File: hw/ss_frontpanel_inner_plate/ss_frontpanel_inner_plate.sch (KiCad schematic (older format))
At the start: 32 parts, among them J1 FFC_conn_14p, J2 FFC_conn_14p, J3 FFC_conn_14p, M1 Mousebite_stamp_holes, M2 Mousebite_stamp_holes, M3 Mousebite_stamp_holes, M4 FFC_retention_clamp, M5 FFC_retention_clamp, U6 TLV9051SIDBV

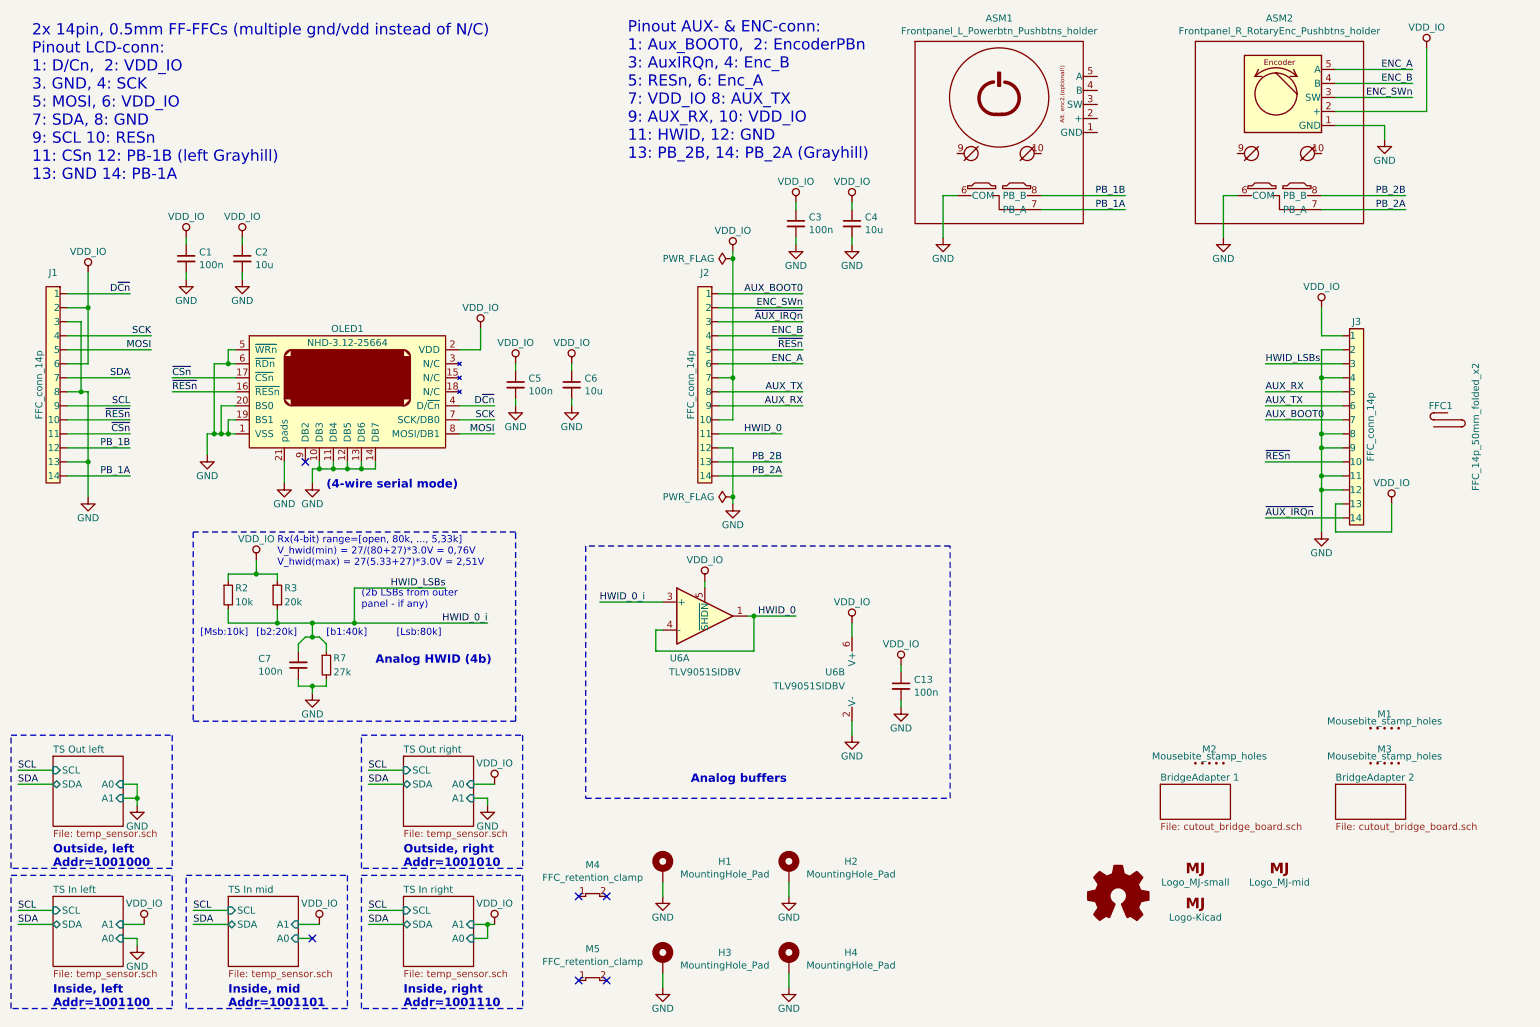
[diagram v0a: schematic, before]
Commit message: Updated display-board sch & PCB with optional left-hand rotary encoder instead of pwrbtn. Printed MB schematic updates PDF for 20-08-21
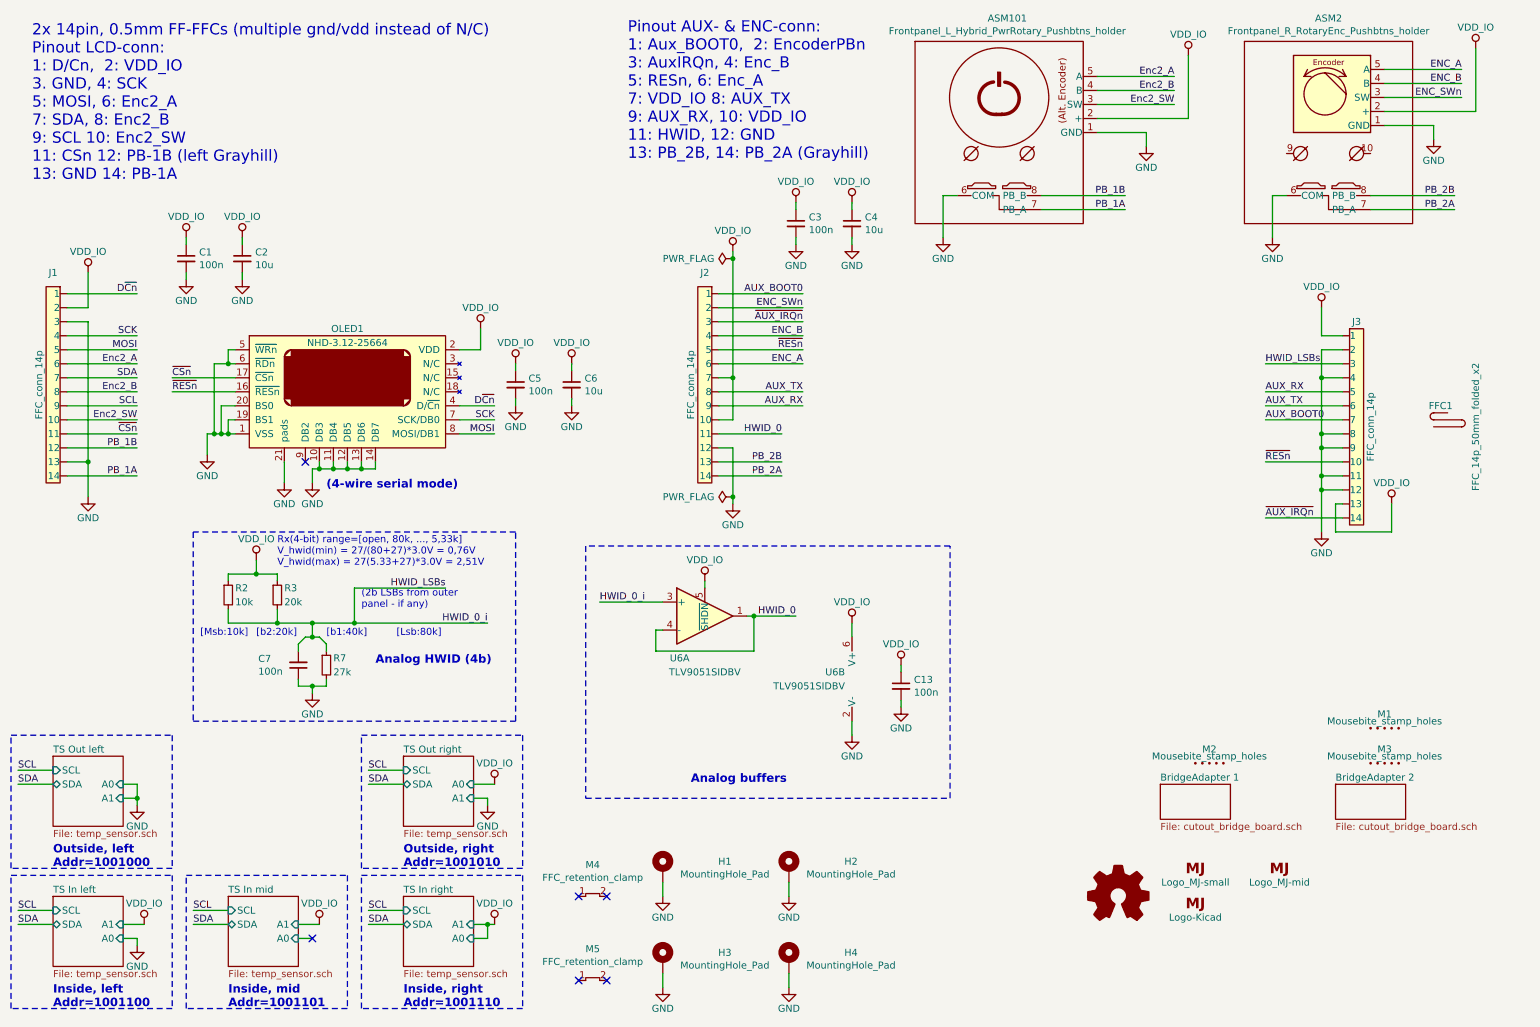
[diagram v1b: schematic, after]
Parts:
- removed ASM1: Frontpanel_L_Powerbtn_Pushbtns_holder, customlib_mj_fp:Frontpanel_L_Powerbtn_Pushbtns_holder, symbol customlib_mj:Frontpanel_L_Powerbtn_Pushbtns_holder
- added ASM101: Frontpanel_L_Hybrid_PwrRotary_Pushbtns_holder, customlib_mj_fp:Frontpanel_L_Hybrid_Power_Rotary_Pushbtns_holder, symbol customlib_mj:Frontpanel_L_Hybrid_PwrRotary_Pushbtns_holder
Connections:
- net GND: now also ASM101.1 (GND), ASM101.6 (COM); no longer J1.8
- net PB_1A: now also ASM101.7 (PB_A)
- net PB_1B: now also ASM101.8 (PB_B)
- net VDD_IO: now also ASM101.2 (+); no longer J1.6
- net ~RESn~: no longer J1.10
- new net Enc2_A: ASM101.5 (A), J1.6
- new net Enc2_B: ASM101.4 (B), J1.8
- new net Enc2_SW: ASM101.3 (SW), J1.10
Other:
- note added: "2x 14pin, 0.5mm FF-FFCs (multiple gnd/vdd instead of N/C)\nPinout LCD-conn:\n1: D/Cn, 2: VDD_IO\n3. GND, 4: SCK\n5: MOSI, 6: Enc2_A\n7: SDA, 8: Enc2_B\n9: SCL 10: Enc2_SW\n11: CSn 12: PB-1B (left Grayhill)\n13: GND 14: PB-1A"
- note removed: "2x 14pin, 0.5mm FF-FFCs (multiple gnd/vdd instead of N/C)\nPinout LCD-conn:\n1: D/Cn, 2: VDD_IO\n3. GND, 4: SCK\n5: MOSI, 6: VDD_IO\n7: SDA, 8: GND\n9: SCL 10: RESn\n11: CSn 12: PB-1B (left Grayhill)\n13: GND 14: PB-1A"
- moved on the sheet: ASM2
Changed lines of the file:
@@
 $EndDescr
 Text Notes 700  1800 0    80   ~ 0
-2x 14pin, 0.5mm FF-FFCs (multiple gnd/vdd instead of N/C)\nPinout LCD-conn:\n1: D/Cn,  2: VDD_IO\n3. GND, 4: SCK\n5: MOSI, 6: VDD_IO\n7: SDA, 8: GND\n9: SCL 10: RESn\n11: CSn 12: PB-1B (left Grayhill)\n13: GND 14: PB-1A
+2x 14pin, 0.5mm FF-FFCs (multiple gnd/vdd instead of N/C)\nPinout LCD-conn:\n1: D/Cn,  2: VDD_IO\n3. GND, 4: SCK\n5: MOSI, 6: Enc2_A\n7: SDA, 8: Enc2_B\n9: SCL 10: Enc2_SW\n11: CSn 12: PB-1B (left Grayhill)\n13: GND 14: PB-1A
 Text Notes 4950 1650 0    80   ~ 0
 Pinout AUX- & ENC-conn:\n1: Aux_BOOT0,  2: EncoderPBn\n3: AuxIRQn, 4: Enc_B\n5: RESn, 6: Enc_A\n7: VDD_IO 8: AUX_TX\n9: AUX_RX, 10: VDD_IO\n11: HWID, 12: GND\n13: PB_2B, 14: PB_2A (Grayhill)
@@
 $EndComp
 $Comp
-L customlib_mj:Frontpanel_L_Powerbtn_Pushbtns_holder ASM1
-U 1 1 5F2241C0
-P 7600 1600
-F 0 "ASM1" H 7600 2565 50  0000 C CNN
-F 1 "Frontpanel_L_Powerbtn_Pushbtns_holder" H 7600 2474 50  0000 C CNN
-F 2 "customlib_mj_fp:Frontpanel_L_Powerbtn_Pushbtns_holder" H 7575 1995 50  0001 C CNN
-F 3 "" H 7575 1995 50  0001 C CNN
-	1    7600 1600
-	1    0    0    -1
-$EndComp
-$Comp
 L customlib_mj:Frontpanel_R_RotaryEnc_Pushbtns_holder ASM2
 U 1 1 5F227C77
-P 9600 1600
-F 0 "ASM2" H 9600 2565 50  0000 C CNN
-F 1 "Frontpanel_R_RotaryEnc_Pushbtns_holder" H 9600 2474 50  0000 C CNN
-F 2 "customlib_mj_fp:Frontpanel_R_RotaryEnc_Pushbtns_holder-one_M3_removed" H 9575 2025 50  0001 C CNN
-F 3 "" H 9575 2025 50  0001 C CNN
-	1    9600 1600
+P 9950 1600
+F 0 "ASM2" H 9950 2565 50  0000 C CNN
+F 1 "Frontpanel_R_RotaryEnc_Pushbtns_holder" H 9950 2474 50  0000 C CNN
+F 2 "customlib_mj_fp:Frontpanel_R_RotaryEnc_Pushbtns_holder-one_M3_removed" H 9925 2025 50  0001 C CNN
+F 3 "" H 9925 2025 50  0001 C CNN
+	1    9950 1600
 	1    0    0    -1
 $EndComp
@@
 $EndComp
 Wire Wire Line
-	950  2900 1550 2900
-Text Label 1550 2900 2    50   ~ 0
+	950  2900 1450 2900
+Text Label 1450 2900 2    50   ~ 0
 SCK
 Wire Wire Line
-	950  3000 1550 3000
+	950  3000 1450 3000
 Wire Wire Line
 	5600 3400 6200 3400
@@
 Wire Wire Line
 	5600 2600 6200 2600
-Text Label 1550 3000 2    50   ~ 0
+Text Label 1450 3000 2    50   ~ 0
 MOSI
-Text Label 1400 3600 2    50   ~ 0
+Text Label 1450 3600 2    50   ~ 0
 ~CSn~
-Text Label 1400 3500 2    50   ~ 0
-~RESn~
 Text Label 6200 3400 2    50   ~ 0
 AUX_RX
@@
 	2750 3850 2850 3850
 Wire Wire Line
-	950  3600 1400 3600
-Wire Wire Line
-	950  3500 1400 3500
+	950  3600 1450 3600
+Wire Wire Line
+	950  3500 1450 3500
 Wire Wire Line
 	2150 3500 2100 3500
@@
 Text Label 4000 3600 2    50   ~ 0
 MOSI
-Text Label 1400 2600 2    50   ~ 0
+Text Label 1450 2600 2    50   ~ 0
 D~Cn~
 $Comp
@@
 $EndComp
 Wire Wire Line
-	950  3900 1400 3900
-Wire Wire Line
-	950  3700 1400 3700
+	950  3900 1450 3900
+Wire Wire Line
+	950  3700 1450 3700
 Wire Wire Line
 	5600 3900 6050 3900
@@
 Wire Wire Line
 	5600 2700 6200 2700
-Text Label 1400 3900 2    50   ~ 0
+Text Label 1450 3900 2    50   ~ 0
 PB_1A
-Text Label 1400 3700 2    50   ~ 0
+Text Label 1450 3700 2    50   ~ 0
 PB_1B
 Text Label 6050 3900 2    50   ~ 0
@@
 	7300 1900 7200 1900
 Wire Wire Line
-	9300 1900 9200 1900
+	9650 1900 9550 1900
 Wire Wire Line
 	7900 1900 8500 1900
@@
 PB_1B
 Wire Wire Line
-	9900 1900 10500 1900
-Wire Wire Line
-	9900 2000 10500 2000
-Text Label 10500 2000 2    50   ~ 0
+	10250 1900 10850 1900
+Wire Wire Line
+	10250 2000 10850 2000
+Text Label 10850 2000 2    50   ~ 0
 PB_2A
-Text Label 10500 1900 2    50   ~ 0
+Text Label 10850 1900 2    50   ~ 0
 PB_2B
 Wire Wire Line
-	10000 1000 10550 1000
-Wire Wire Line
-	10000 1100 10550 1100
-Wire Wire Line
-	10000 1200 10550 1200
-Text Label 10550 1000 2    50   ~ 0
+	10350 1000 10900 1000
+Wire Wire Line
+	10350 1100 10900 1100
+Wire Wire Line
+	10350 1200 10900 1200
+Text Label 10900 1000 2    50   ~ 0
 ENC_A
-Text Label 10550 1100 2    50   ~ 0
+Text Label 10900 1100 2    50   ~ 0
 ENC_B
-Text Label 10550 1200 2    50   ~ 0
+Text Label 10900 1200 2    50   ~ 0
 ENC_SWn
 $Comp
 L customlib_mj:VDD_IO #PWR01
 U 1 1 5F436C13
-P 10650 850
-F 0 "#PWR01" H 10650 700 50  0001 C CNN
-F 1 "VDD_IO" H 10650 1000 50  0000 C CNN
-F 2 "" H 10650 850 50  0001 C CNN
-F 3 "" H 10650 850 50  0001 C CNN
-	1    10650 850
-	1    0    0    -1
-$EndComp
-Wire Wire Line
-	10650 850  10650 1300
-Wire Wire Line
-	10650 1300 10000 1300
+P 11000 850
+F 0 "#PWR01" H 11000 700 50  0001 C CNN
+F 1 "VDD_IO" H 11000 1000 50  0000 C CNN
+F 2 "" H 11000 850 50  0001 C CNN
+F 3 "" H 11000 850 50  0001 C CNN
+	1    11000 850
+	1    0    0    -1
+$EndComp
+Wire Wire Line
+	11000 850  11000 1300
+Wire Wire Line
+	11000 1300 10350 1300
 Text Label 4000 3400 2    50   ~ 0
 D~Cn~
@@
 	5700 3700 5700 4050
 Wire Wire Line
-	950  3200 1400 3200
-Wire Wire Line
-	950  3400 1400 3400
-Text Label 1400 3200 2    50   ~ 0
+	950  3200 1450 3200
+Wire Wire Line
+	950  3400 1450 3400
+Text Label 1450 3200 2    50   ~ 0
 SDA
-Text Label 1400 3400 2    50   ~ 0
+Text Label 1450 3400 2    50   ~ 0
 SCL
 $Comp
@@
 L power:GND #PWR014
 U 1 1 5F47CC32
-P 9200 2200
-F 0 "#PWR014" H 9200 1950 50  0001 C CNN
-F 1 "GND" H 9200 2050 50  0000 C CNN
-F 2 "" H 9200 2200 50  0001 C CNN
-F 3 "" H 9200 2200 50  0001 C CNN
-	1    9200 2200
-	1    0    0    -1
-$EndComp
-Wire Wire Line
-	9200 1900 9200 2200
+P 9550 2200
+F 0 "#PWR014" H 9550 1950 50  0001 C CNN
+F 1 "GND" H 9550 2050 50  0000 C CNN
+F 2 "" H 9550 2200 50  0001 C CNN
+F 3 "" H 9550 2200 50  0001 C CNN
+	1    9550 2200
+	1    0    0    -1
+$EndComp
+Wire Wire Line
+	9550 1900 9550 2200
 Wire Wire Line
 	7200 2200 7200 1900
@@
 L power:GND #PWR02
 U 1 1 5F485434
-P 10350 1500
-F 0 "#PWR02" H 10350 1250 50  0001 C CNN
-F 1 "GND" H 10350 1350 50  0000 C CNN
-F 2 "" H 10350 1500 50  0001 C CNN
-F 3 "" H 10350 1500 50  0001 C CNN
-	1    10350 1500
-	1    0    0    -1
-$EndComp
-Wire Wire Line
-	10350 1500 10350 1400
-Wire Wire Line
-	10350 1400 10000 1400
+P 10700 1500
+F 0 "#PWR02" H 10700 1250 50  0001 C CNN
+F 1 "GND" H 10700 1350 50  0000 C CNN
+F 2 "" H 10700 1500 50  0001 C CNN
+F 3 "" H 10700 1500 50  0001 C CNN
+	1    10700 1500
+	1    0    0    -1
+$EndComp
+Wire Wire Line
+	10700 1500 10700 1400
+Wire Wire Line
+	10700 1400 10350 1400
 $Comp
 L power:GND #PWR022
@@
 ~CSn~
 Wire Wire Line
-	950  2600 1400 2600
+	950  2600 1450 2600
 Text Label 6200 3000 2    50   ~ 0
 ~RESn~
 Wire Wire Line
 	5600 3000 6200 3000
-Wire Wire Line
-	950  3300 1050 3300
-Wire Wire Line
-	1100 3300 1100 3800
-Wire Wire Line
-	950  3100 1100 3100
 Wire Wire Line
 	5700 3200 5600 3200
@@
 Wire Wire Line
 	950  2700 1100 2700
-Connection ~ 1100 2700
 Wire Wire Line
 	1100 2700 1100 2450
@@
 Connection ~ 5700 3200
 Wire Wire Line
-	1100 2700 1100 3100
-Wire Wire Line
-	950  2800 1050 2800
-Wire Wire Line
-	1050 2800 1050 3300
-Connection ~ 1050 3300
-Wire Wire Line
-	1050 3300 1100 3300
+	950  2800 1100 2800
 Wire Wire Line
 	950  3800 1100 3800
@@
 Wire Wire Line
 	1100 3800 1100 4050
+Text Label 1450 3500 2    50   ~ 0
+Enc2_SW
+Wire Wire Line
+	1100 2800 1100 3800
+Wire Wire Line
+	950  3100 1450 3100
+Wire Wire Line
+	950  3300 1450 3300
+Text Label 1450 3100 2    50   ~ 0
+Enc2_A
+Text Label 1450 3300 2    50   ~ 0
+Enc2_B
+$Comp
+L customlib_mj:Frontpanel_L_Hybrid_PwrRotary_Pushbtns_holder ASM101
+U 1 1 5FCBCA58
+P 7600 1600
+F 0 "ASM101" H 7658 2565 50  0000 C CNN
+F 1 "Frontpanel_L_Hybrid_PwrRotary_Pushbtns_holder" H 7658 2474 50  0000 C CNN
+F 2 "customlib_mj_fp:Frontpanel_L_Hybrid_Power_Rotary_Pushbtns_holder" H 7575 1995 50  0001 C CNN
+F 3 "" H 7575 1995 50  0001 C CNN
+	1    7600 1600
+	1    0    0    -1
+$EndComp
+$Comp
+L power:GND #PWR0106
+U 1 1 5FCC0149
+P 8650 1550
+F 0 "#PWR0106" H 8650 1300 50  0001 C CNN
+F 1 "GND" H 8650 1400 50  0000 C CNN
+F 2 "" H 8650 1550 50  0001 C CNN
+F 3 "" H 8650 1550 50  0001 C CNN
+	1    8650 1550
+	1    0    0    -1
+$EndComp
+Wire Wire Line
+	8650 1550 8650 1450
+Wire Wire Line
+	8650 1450 8300 1450
+Wire Wire Line
+	8300 1050 8850 1050
+Wire Wire Line
+	8300 1150 8850 1150
+Wire Wire Line
+	8300 1250 8850 1250
+Text Label 8850 1050 2    50   ~ 0
+Enc2_A
+Text Label 8850 1150 2    50   ~ 0
+Enc2_B
+Text Label 8850 1250 2    50   ~ 0
+Enc2_SW
+$Comp
+L customlib_mj:VDD_IO #PWR0105
+U 1 1 5FCCA10E
+P 8950 900
+F 0 "#PWR0105" H 8950 750 50  0001 C CNN
+F 1 "VDD_IO" H 8950 1050 50  0000 C CNN
+F 2 "" H 8950 900 50  0001 C CNN
+F 3 "" H 8950 900 50  0001 C CNN
+	1    8950 900
+	1    0    0    -1
+$EndComp
+Wire Wire Line
+	8950 900  8950 1350
+Wire Wire Line
+	8950 1350 8300 1350
 $EndSCHEMATC

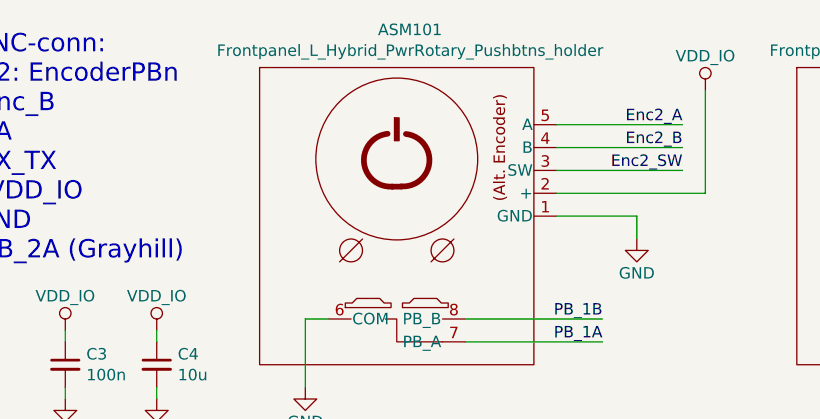
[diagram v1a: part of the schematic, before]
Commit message: Updated display-board with mech updates. Default version is original left PwrBtn + right Rotary
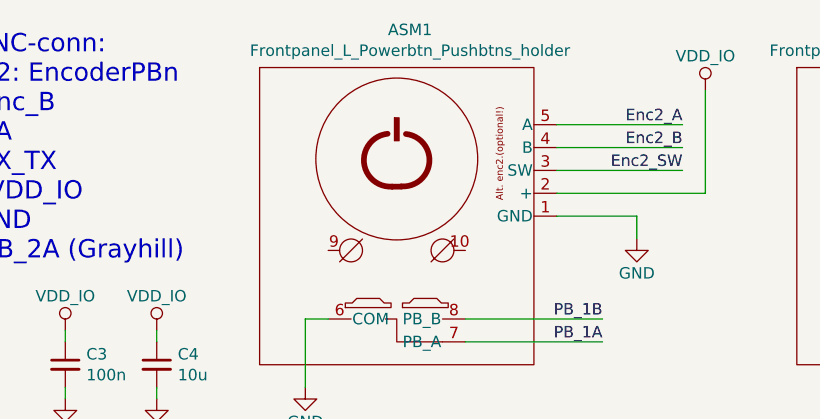
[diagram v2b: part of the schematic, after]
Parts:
- removed ASM101: Frontpanel_L_Hybrid_PwrRotary_Pushbtns_holder, customlib_mj_fp:Frontpanel_L_Hybrid_Power_Rotary_Pushbtns_holder, symbol customlib_mj:Frontpanel_L_Hybrid_PwrRotary_Pushbtns_holder
- added ASM1: Frontpanel_L_Powerbtn_Pushbtns_holder, customlib_mj_fp:Frontpanel_L_Powerbtn_Pushbtns_holder, symbol customlib_mj:Frontpanel_L_Powerbtn_Pushbtns_holder
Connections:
- net Enc2_A: now also ASM1.5 (A)
- net Enc2_B: now also ASM1.4 (B)
- net Enc2_SW: now also ASM1.3 (SW)
- net GND: now also ASM1.1 (GND), ASM1.6 (COM)
- net PB_1A: now also ASM1.7 (PB_A)
- net PB_1B: now also ASM1.8 (PB_B)
- net VDD_IO: now also ASM1.2 (+)
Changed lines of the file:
@@
 Enc2_B
-$Comp
-L customlib_mj:Frontpanel_L_Hybrid_PwrRotary_Pushbtns_holder ASM101
-U 1 1 5FCBCA58
-P 7600 1600
-F 0 "ASM101" H 7658 2565 50  0000 C CNN
-F 1 "Frontpanel_L_Hybrid_PwrRotary_Pushbtns_holder" H 7658 2474 50  0000 C CNN
-F 2 "customlib_mj_fp:Frontpanel_L_Hybrid_Power_Rotary_Pushbtns_holder" H 7575 1995 50  0001 C CNN
-F 3 "" H 7575 1995 50  0001 C CNN
-	1    7600 1600
-	1    0    0    -1
-$EndComp
 $Comp
 L power:GND #PWR0106
@@
 Wire Wire Line
 	8950 1350 8300 1350
+$Comp
+L customlib_mj:Frontpanel_L_Powerbtn_Pushbtns_holder ASM1
+U 1 1 5F4694CB
+P 7600 1600
+F 0 "ASM1" H 7658 2565 50  0000 C CNN
+F 1 "Frontpanel_L_Powerbtn_Pushbtns_holder" H 7658 2474 50  0000 C CNN
+F 2 "customlib_mj_fp:Frontpanel_L_Powerbtn_Pushbtns_holder" H 7575 1995 50  0001 C CNN
+F 3 "" H 7575 1995 50  0001 C CNN
+	1    7600 1600
+	1    0    0    -1
+$EndComp
 $EndSCHEMATC
